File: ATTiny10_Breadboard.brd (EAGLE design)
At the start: 16 x 24 mm, 5 parts, among them IC1 ATTINY4/5/9/10, J1 ISP/TPI-6PIN

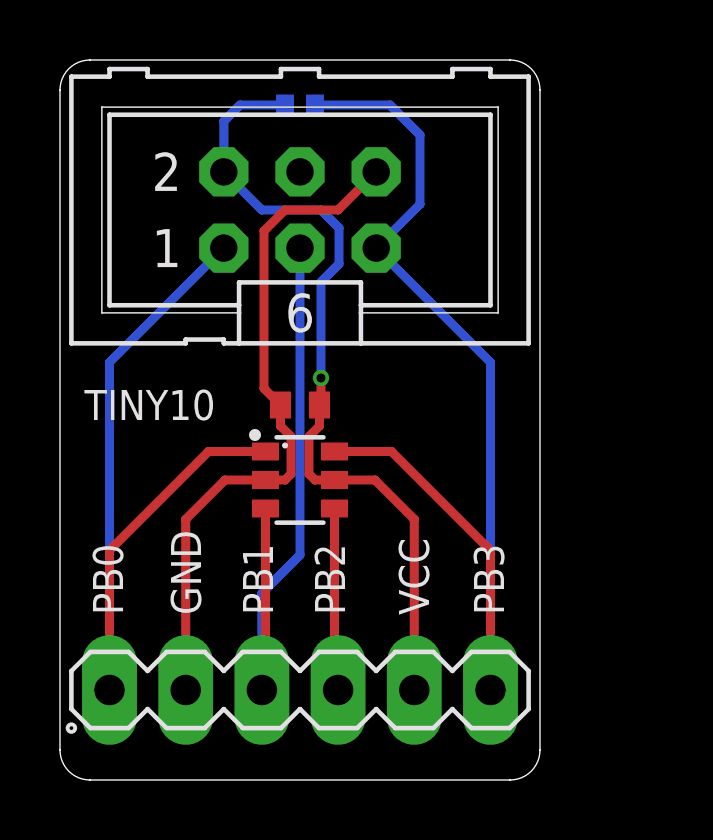
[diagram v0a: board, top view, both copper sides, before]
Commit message: Fixed Tiny10 Board: Now there's an option to connect MISO and MOSI for USBasp compatibility
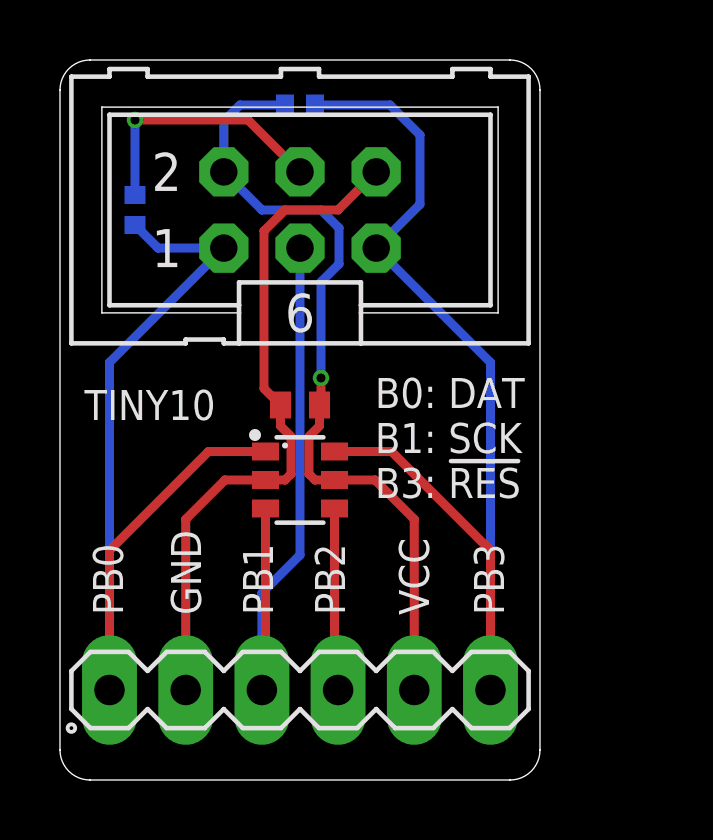
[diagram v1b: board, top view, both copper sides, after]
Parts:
- added R2: 0R, rcl:R0402
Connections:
- new net N$1: J1.4, R2.2
- net PB0: now also R2.1
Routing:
- net N$1: track 0.00 -> 8.72 mm, vias 0 -> 1
- net PB0: track 27.5 -> 30.8 mm
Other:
- board text added: "B0: DAT B1: SCK B3: !RES!"
- board text added: "Close R2 for USBasp"
